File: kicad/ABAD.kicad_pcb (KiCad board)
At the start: 2 copper layers, 5 parts, among them U1 MS5611-01BA, U2 ESP32-WROOM-32, U3 MPU-6050

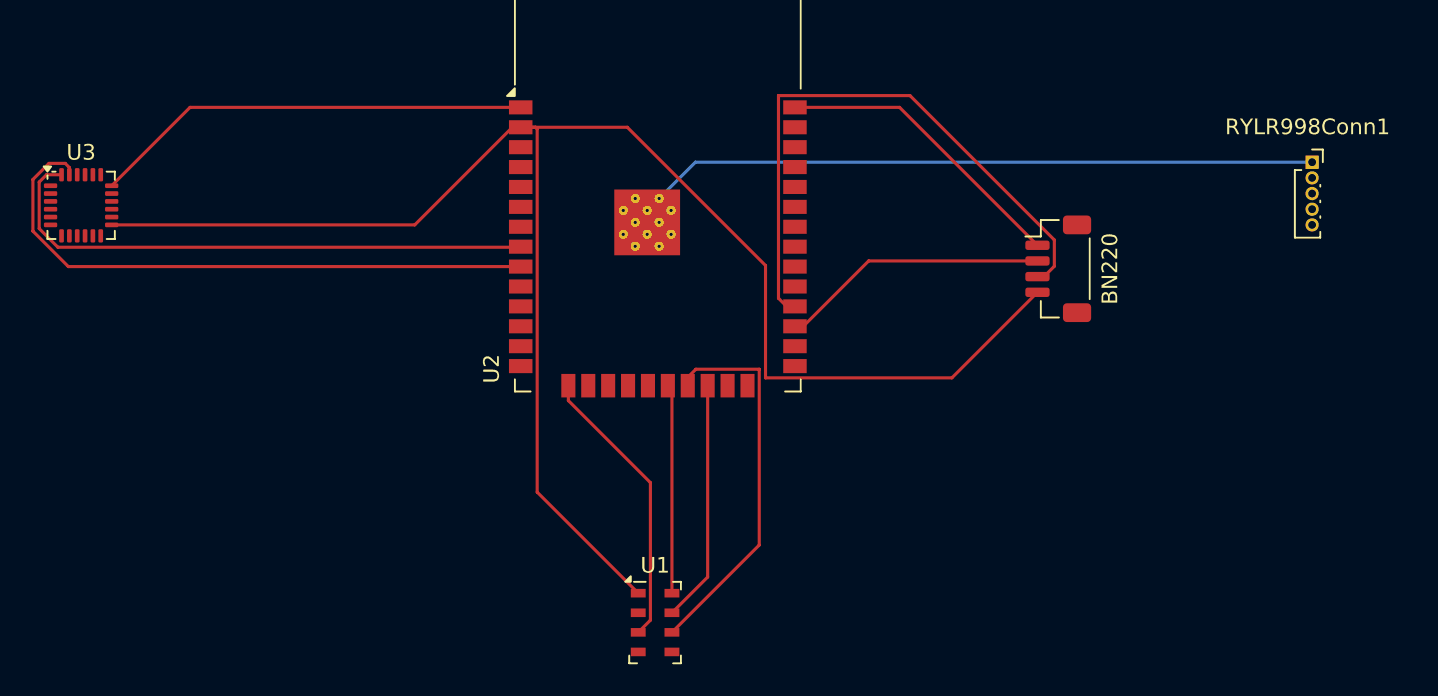
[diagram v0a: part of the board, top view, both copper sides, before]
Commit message: Completed first iteration of fc pcb
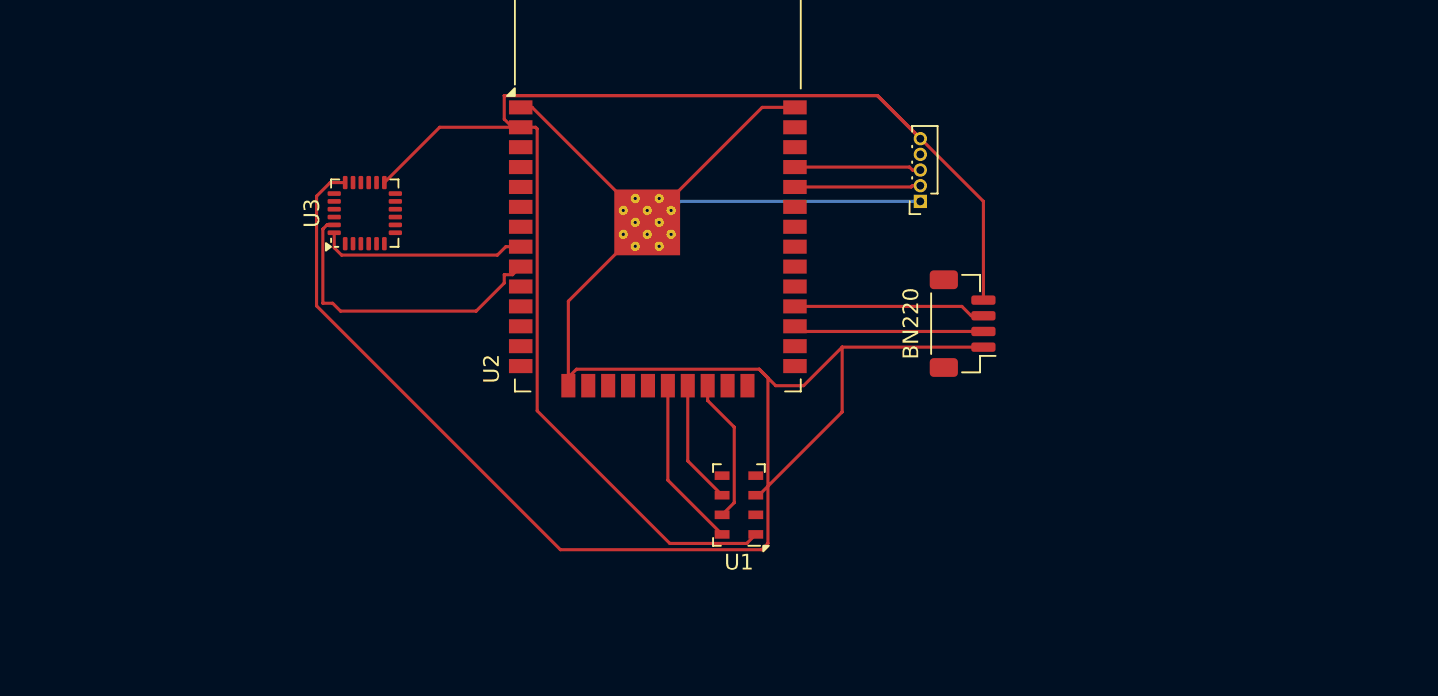
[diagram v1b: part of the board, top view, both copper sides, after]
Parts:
- moved RYLR998Conn1 25.1 mm to (145.0, 102.0), turned to 180 degrees
- moved U3 18.1 mm to (109.5, 102.8), turned to 90 degrees
- moved U1 9.21 mm to (133.4, 121.4), turned to 180 degrees
- moved BN220 7.03 mm to (147.7, 109.8), turned to 90 degrees
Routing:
- net /GND: track 108.1 -> 142.2 mm
- net /RX1: track 38.6 -> 12.8 mm
- net Net-(U2-IO32): track 35.8 -> 13.3 mm
- net Net-(U2-IO33): track 38.7 -> 19.9 mm
- net Net-(U1-SDO): track 24.4 -> 8.43 mm
- net /VCC: track 108.1 -> 117.1 mm
- net /RX0: track 0.00 -> 8.08 mm
- net /TX0: track 0.00 -> 8.03 mm
- net Net-(U1-SDI/SDA): track 15.4 -> 9.26 mm
- net /TX1: track 17.2 -> 12.7 mm
- net Net-(U1-SCLK): track 13.3 -> 11.3 mm

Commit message: Gerber and other output files
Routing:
- net Net-(U1-CSB-Pad4): track 0.00 -> 2.15 mm
- net Net-(U1-SDI/SDA): track 9.26 -> 9.43 mm, vias 0 -> 2
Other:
- board outline added: 47 x 36.5 mm
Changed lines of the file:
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@@
 			(outputformat 1)
 			(mirror no)
-			(drillshape 1)
+			(drillshape 0)
 			(scaleselection 1)
-			(outputdirectory "")
+			(outputdirectory "outputs/")
 		)
 	)
@@
 		)
 	)
+	(gr_rect
+		(start 105 88)
+		(end 152 124.5)
+		(stroke
+			(width 0.05)
+			(type default)
+		)
+		(fill no)
+		(layer "Edge.Cuts")
+	)
 	(segment
 		(start 132.35 123.25)
@@
 	)
 	(segment
-		(start 133.126 121.224)
-		(end 133.126 116.406)
+		(start 134.5 119.5)
+		(end 132.35 119.5)
 		(width 0.2)
 		(layer "F.Cu")
-		(net 3)
+		(net 2)
 	)
 	(segment
-		(start 132.35 122)
-		(end 133.126 121.224)
+		(start 133.325002 121.024998)
+		(end 133.325002 120.5)
 		(width 0.2)
 		(layer "F.Cu")
@@
 	)
 	(segment
+		(start 132.35 122)
+		(end 133.325002 121.024998)
+		(width 0.2)
+		(layer "F.Cu")
+		(net 3)
+	)
+	(segment
 		(start 133.126 116.406)
 		(end 131.43 114.71)
@@
 		(net 3)
 	)
+	(via
+		(at 133.126 116.406)
+		(size 0.6)
+		(drill 0.3)
+		(layers "F.Cu" "B.Cu")
+		(net 3)
+	)
+	(via
+		(at 133.325002 120.5)
+		(size 0.6)
+		(drill 0.3)
+		(layers "F.Cu" "B.Cu")
+		(net 3)
+	)
+	(segment
+		(start 133.126 120.300998)
+		(end 133.126 116.406)
+		(width 0.2)
+		(layer "B.Cu")
+		(net 3)
+	)
+	(segment
+		(start 133.325002 120.5)
+		(end 133.126 120.300998)
+		(width 0.2)
+		(layer "B.Cu")
+		(net 3)
+	)

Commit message: ESD array and Net labels fixed
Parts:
- removed BN220: Conn_01x04, Connector_JST:JST_SH_BM04B-SRSS-TB_1x04-1MP_P1.00mm_Vertical
- removed RYLR998Conn1: Conn_01x05, Connector_PinSocket_1.00mm:PinSocket_1x05_P1.00mm_Vertical
- removed U1: MS5611-01BA, Package_LGA:LGA-8_3x5mm_P1.25mm
- removed U2: ESP32-WROOM-32, RF_Module:ESP32-WROOM-32
- removed U3: MPU-6050, Sensor_Motion:InvenSense_QFN-24_4x4mm_P0.5mm
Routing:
- net /GND: track 142.2 -> 0.00 mm
- net /VCC: track 117.1 -> 0.00 mm
- net Net-(U2-IO33): track 19.9 -> 0.00 mm
- net Net-(U2-IO32): track 13.3 -> 0.00 mm
- net /RX1: track 12.8 -> 0.00 mm
- net /TX1: track 12.7 -> 0.00 mm
- net Net-(U1-SCLK): track 11.3 -> 0.00 mm
- net Net-(U1-SDI/SDA): track 9.43 -> 0.00 mm, vias 2 -> 0
- net Net-(U1-SDO): track 8.43 -> 0.00 mm
- net /RX0: track 8.08 -> 0.00 mm
- net /TX0: track 8.03 -> 0.00 mm
- net Net-(U1-CSB-Pad4): track 2.15 -> 0.00 mm
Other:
- board outline removed

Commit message: 4 layer PCB design - now deprecated due to high production cost
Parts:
- added C1: 100nF, Capacitor_SMD:C_0805_2012Metric, F.Cu at (161.6, 105.0)
- added C10: 10uF, Capacitor_SMD:C_0805_2012Metric, F.Cu at (143.5, 107.7)
- added C11: 10uF, Capacitor_SMD:C_0805_2012Metric, F.Cu at (137.5, 99.9)
- added C12: 10nF, 4V, Capacitor_SMD:C_0805_2012Metric, F.Cu at (159.4, 101.4)
- added C13: 0.1uF, 4V, Capacitor_SMD:C_0805_2012Metric, F.Cu at (161.6, 101.3)
- added C14: 100nF, Capacitor_SMD:C_0805_2012Metric, F.Cu at (152.6, 76.2)
- added C15: 0.1uF, 2V, Capacitor_SMD:C_0805_2012Metric, F.Cu at (153.5, 106.2)
- added C16: 2.2nF, 50V, Capacitor_SMD:C_0805_2012Metric, F.Cu at (155.2, 97.9)
- added C17: 22uF, Capacitor_SMD:C_0805_2012Metric, F.Cu at (132.0, 53.5)
- added C18: 0.1uF, Capacitor_SMD:C_0805_2012Metric, F.Cu at (134.6, 53.5)
- added C2: 10uF, Capacitor_SMD:C_0805_2012Metric, F.Cu at (159.3, 105.0)
- added C3: 10uF 6.3V, Capacitor_SMD:C_0805_2012Metric, F.Cu at (134.5, 99.0)
- added C4: 0.1uF, Capacitor_SMD:C_0805_2012Metric, F.Cu at (134.0, 107.5)
- added C7: 1uF, Capacitor_SMD:C_0805_2012Metric, F.Cu at (132.0, 57.2)
- added C8: 0.1uF, Capacitor_SMD:C_0805_2012Metric, F.Cu at (158.6, 67.9)
- added C9: 10uF, Capacitor_SMD:C_0805_2012Metric, F.Cu at (139.7, 99.9)
- added D1: D_Schottky, Diode_SMD:D_3220_8050Metric, F.Cu at (144.9, 114.3)
- added D2: RF_LED_GREEN, LED_SMD:LED_0805_2012Metric, F.Cu at (142.6, 78.6)
- added D3: GPS_LED_BLUE, LED_SMD:LED_0805_2012Metric, F.Cu at (142.6, 76.1)
- added D4: PWR_LED_RED, LED_SMD:LED_0805_2012Metric, F.Cu at (142.5, 73.5)
- added H1: MountingHole, MountingHole:MountingHole_3.2mm_M3_Pad, F.Cu at (131.9, 124.6)
- added H2: MountingHole, MountingHole:MountingHole_3.2mm_M3_Pad, F.Cu at (161.1, 54.2)
- added J1: Edge mounted SMA, Connector_Coaxial:SMA_Molex_73251-1153_EdgeMount_Horizontal, F.Cu at (141.6, 122.5)
- added J2: USB_C_Receptacle_USB2.0_16P, Connector_USB:USB_C_Receptacle_GCT_USB4105-xx-A_16P_TopMnt_Horizontal, F.Cu at (132.1, 91.5)
- added J3: BATT Screw Terminal, TerminalBlock_MetzConnect:TerminalBlock_MetzConnect_Type055_RT01502HDWU_1x02_P5.00mm_Horizontal, F.Cu at (132.8, 116.6)
- added L1: 1.5A 2.2uH, Inductor_SMD:L_0805_2012Metric, F.Cu at (134.5, 100.9)
- added Q1: AO3401A, Package_TO_SOT_SMD:SOT-23, F.Cu at (139.7, 114.4)
- added Q2: AO3401A, Package_TO_SOT_SMD:SOT-23, F.Cu at (139.7, 108.4)
- added R1: 5.1k, Resistor_SMD:R_0805_2012Metric, F.Cu at (138.1, 83.4)
- added R10: 68, Resistor_SMD:R_0805_2012Metric, F.Cu at (138.6, 73.6)
- added R11: 10k, Resistor_SMD:R_0805_2012Metric, F.Cu at (160.1, 76.2)
- added R12: 10k, Resistor_SMD:R_0805_2012Metric, F.Cu at (162.1, 76.2)
- added R13: 10k, Resistor_SMD:R_0805_2012Metric, F.Cu at (149.0, 101.3)
- added R14: 10k, Resistor_SMD:R_0805_2012Metric, F.Cu at (147.0, 101.3)
- added R2: 5.1k, Resistor_SMD:R_0805_2012Metric, F.Cu at (140.4, 93.3)
- added R3: 100Ω, Resistor_SMD:R_0805_2012Metric, F.Cu at (130.5, 104.2)
- added R4: 22Ω, Resistor_SMD:R_0805_2012Metric, F.Cu at (140.2, 83.4)
- added R5: 22Ω, Resistor_SMD:R_0805_2012Metric, F.Cu at (142.2, 83.4)
- added R6: 10k, Resistor_SMD:R_0805_2012Metric, F.Cu at (134.5, 57.2)
- added R7: 10k, Resistor_SMD:R_0805_2012Metric, F.Cu at (158.6, 65.4)
- added R8: 68, Resistor_SMD:R_0805_2012Metric, F.Cu at (138.6, 78.5)
- added R9: 68, Resistor_SMD:R_0805_2012Metric, F.Cu at (138.6, 76.1)
- added RESET_SW1: SW_Push, Button_Switch_THT:SW_PUSH_1P1T_6x3.5mm_H4.3_APEM_MJTP1243, F.Cu at (131.9, 62.8)
- added RESET_SW2: SW_Push, Button_Switch_THT:SW_PUSH_1P1T_6x3.5mm_H4.3_APEM_MJTP1243, F.Cu at (162.6, 63.0)
- added TP1: TXD0, TestPoint:TestPoint_Pad_D1.0mm, F.Cu at (161.0, 60.1)
- added TP2: RXD0, TestPoint:TestPoint_Pad_D1.0mm, F.Cu at (158.3, 60.1)
- added TP3: 3.3V, TestPoint:TestPoint_Pad_D1.0mm, F.Cu at (143.1, 96.9)
- added TP4: VBUS, TestPoint:TestPoint_Pad_D1.0mm, F.Cu at (139.7, 96.8)
- added TP5: BATT+, TestPoint:TestPoint_Pad_D1.0mm, F.Cu at (130.7, 99.3)
- added TP6: BATT_RAW+, TestPoint:TestPoint_Pad_D1.0mm, F.Cu at (137.9, 103.3)
- added TP7: GND, TestPoint:TestPoint_Pad_D1.0mm, F.Cu at (140.7, 103.3)
- added U1: ~, Lora1262:WIRELM-SMD_16P-L16.0-W16.0-P2.00_LORA-CC68-915MHZ-TCXO, F.Cu at (156.4, 117.1)
- added U2: ESP32-S3-WROOM-1, RF_Module:ESP32-S3-WROOM-1, F.Cu at (146.6, 56.9)
- added U3: USBLC6-2SC6, Package_TO_SOT_SMD:SOT-23-6, F.Cu at (141.0, 87.6)
- added U4: TPS63001, Package_SON:Texas_DRC0010J_ThermalVias, F.Cu at (134.3, 104.4)
- added U6: MPU-6050, Sensor_Motion:InvenSense_QFN-24_4x4mm_P0.5mm, F.Cu at (153.4, 102.1)
- added U7: MS5611-01BA, Package_LGA:LGA-8_3x5mm_P1.25mm, F.Cu at (156.0, 75.8)
- added U8: L80-R, RF_GPS:Quectel_L80-R, F.Cu at (155.2, 88.3)
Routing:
- net /ACCEL_SDA: track 0.00 -> 81.3 mm, vias 0 -> 2
- net /NSS: track 0.00 -> 80.7 mm, vias 0 -> 2
- net /NRESET: track 0.00 -> 65.9 mm, vias 0 -> 2
- net /SCLK: track 0.00 -> 65.3 mm, vias 0 -> 2
- net /MISO: track 0.00 -> 63.1 mm, vias 0 -> 2
- net /MOSI: track 0.00 -> 62.0 mm, vias 0 -> 2
- net +3.3V: track 0.00 -> 60.8 mm, vias 0 -> 15
- net /ACCEL_SCL: track 0.00 -> 54.5 mm, vias 0 -> 2
- net /TXCO: track 0.00 -> 46.1 mm, vias 0 -> 2
- net VBUS: track 0.00 -> 45.3 mm, vias 0 -> 2
- net /BUSY: track 0.00 -> 43.5 mm, vias 0 -> 2
- net /PPS: track 0.00 -> 43.3 mm, vias 0 -> 3
- net /RF_INT: track 0.00 -> 42.7 mm, vias 0 -> 2
- net /ACCEL_INT: track 0.00 -> 42.3 mm, vias 0 -> 2
- net /BARO_SDA: track 0.00 -> 36.9 mm, vias 0 -> 2
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- added copper zone on In2.Cu, net +3.3V
- added copper zone on B.Cu, net GND
- added copper zone on F.Cu, net GND
- added copper zone on In1.Cu, net GND
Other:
- board outline added: 36.9 x 85.2 mm
- copper layers 2 -> 4
- board text added: "BOOT"
- board text added: "EN"
- board text added: "PPS LED"
- board text added: "PWR LED"
- board text added: "RF LED"
